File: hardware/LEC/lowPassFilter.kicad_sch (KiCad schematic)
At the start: 3 parts

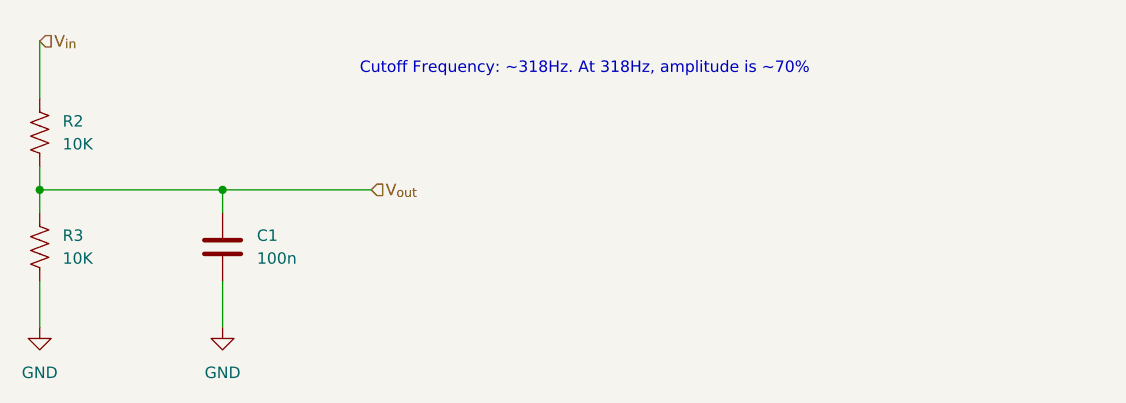
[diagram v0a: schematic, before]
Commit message: Updated LVR selection and other optimizations. Need to update footprints and symbols
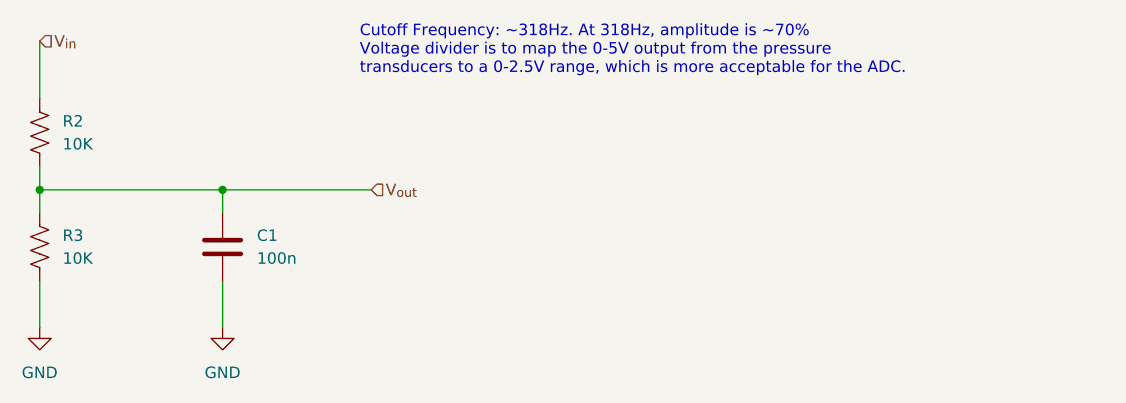
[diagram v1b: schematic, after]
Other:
- note added: "Cutoff Frequency: ~318Hz. At 318Hz, amplitude is ~70% Voltage divider is to map the 0-5V output from the pressure transducers to a 0-2.5V range, which is more acceptable for the ADC."
- note removed: "Cutoff Frequency: ~318Hz. At 318Hz, amplitude is ~70%"
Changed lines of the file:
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@@
     (stroke (width 0) (type default))
   )
-  (text "Cutoff Frequency: ~318Hz. At 318Hz, amplitude is ~70%"
+  (text "Cutoff Frequency: ~318Hz. At 318Hz, amplitude is ~70%\nVoltage divider is to map the 0-5V output from the pressure\ntransducers to a 0-2.5V range, which is more acceptable for the ADC."
     (at 88.9 45.72 0)
     (effects (font (size 1.27 1.27)) (justify left bottom))
@@
           (reference "R3") (unit 1)
         )
+        (path "/c984ce56-a2b4-4cda-8793-153280694173/43e0f5e3-3f54-4d98-bbaa-462e93d257d8"
+          (reference "R4") (unit 1)
+        )
+        (path "/c984ce56-a2b4-4cda-8793-153280694173/c8421286-eac1-4319-8828-3ae62d6cf309"
+          (reference "R6") (unit 1)
+        )
+        (path "/c984ce56-a2b4-4cda-8793-153280694173/7d537dc8-0a6f-4081-8b44-5517c0a70636"
+          (reference "R8") (unit 1)
+        )
+        (path "/c984ce56-a2b4-4cda-8793-153280694173/22bc0796-a1d2-4bdd-adaf-c9789f8654bb"
+          (reference "R10") (unit 1)
+        )
+        (path "/c984ce56-a2b4-4cda-8793-153280694173/ddbe9da2-a7af-420b-9885-57c1b56df261"
+          (reference "R12") (unit 1)
+        )
+        (path "/c984ce56-a2b4-4cda-8793-153280694173/f0feb978-fa39-4938-b0b7-0afa0feb56b9"
+          (reference "R14") (unit 1)
+        )
       )
     )
@@
           (reference "R2") (unit 1)
         )
+        (path "/c984ce56-a2b4-4cda-8793-153280694173/43e0f5e3-3f54-4d98-bbaa-462e93d257d8"
+          (reference "R1") (unit 1)
+        )
+        (path "/c984ce56-a2b4-4cda-8793-153280694173/c8421286-eac1-4319-8828-3ae62d6cf309"
+          (reference "R5") (unit 1)
+        )
+        (path "/c984ce56-a2b4-4cda-8793-153280694173/7d537dc8-0a6f-4081-8b44-5517c0a70636"
+          (reference "R7") (unit 1)
+        )
+        (path "/c984ce56-a2b4-4cda-8793-153280694173/22bc0796-a1d2-4bdd-adaf-c9789f8654bb"
+          (reference "R9") (unit 1)
+        )
+        (path "/c984ce56-a2b4-4cda-8793-153280694173/ddbe9da2-a7af-420b-9885-57c1b56df261"
+          (reference "R11") (unit 1)
+        )
+        (path "/c984ce56-a2b4-4cda-8793-153280694173/f0feb978-fa39-4938-b0b7-0afa0feb56b9"
+          (reference "R13") (unit 1)
+        )
       )
     )
@@
           (reference "C1") (unit 1)
         )
+        (path "/c984ce56-a2b4-4cda-8793-153280694173/43e0f5e3-3f54-4d98-bbaa-462e93d257d8"
+          (reference "C4") (unit 1)
+        )
+        (path "/c984ce56-a2b4-4cda-8793-153280694173/c8421286-eac1-4319-8828-3ae62d6cf309"
+          (reference "C5") (unit 1)
+        )
+        (path "/c984ce56-a2b4-4cda-8793-153280694173/7d537dc8-0a6f-4081-8b44-5517c0a70636"
+          (reference "C6") (unit 1)
+        )
+        (path "/c984ce56-a2b4-4cda-8793-153280694173/22bc0796-a1d2-4bdd-adaf-c9789f8654bb"
+          (reference "C7") (unit 1)
+        )
+        (path "/c984ce56-a2b4-4cda-8793-153280694173/ddbe9da2-a7af-420b-9885-57c1b56df261"
+          (reference "C8") (unit 1)
+        )
+        (path "/c984ce56-a2b4-4cda-8793-153280694173/f0feb978-fa39-4938-b0b7-0afa0feb56b9"
+          (reference "C9") (unit 1)
+        )
       )
     )
@@
   (symbol (lib_id "power:GND") (at 53.34 73.66 0) (unit 1)
     (in_bom yes) (on_board yes) (dnp no) (fields_autoplaced)
-    (property "Reference" "#PWR016" (at 53.34 80.01 0)
+    (property "Reference" "#PWR049" (at 53.34 80.01 0)
       (effects (font (size 1.27 1.27)) hide)
     )
@@
       (project "LEC"
         (path "/c984ce56-a2b4-4cda-8793-153280694173/0e5671ea-d349-45f8-bf6b-96c457441257"
+          (reference "#PWR049") (unit 1)
+        )
+        (path "/c984ce56-a2b4-4cda-8793-153280694173/43e0f5e3-3f54-4d98-bbaa-462e93d257d8"
+          (reference "#PWR03") (unit 1)
+        )
+        (path "/c984ce56-a2b4-4cda-8793-153280694173/c8421286-eac1-4319-8828-3ae62d6cf309"
+          (reference "#PWR04") (unit 1)
+        )
+        (path "/c984ce56-a2b4-4cda-8793-153280694173/7d537dc8-0a6f-4081-8b44-5517c0a70636"
           (reference "#PWR016") (unit 1)
+        )
+        (path "/c984ce56-a2b4-4cda-8793-153280694173/22bc0796-a1d2-4bdd-adaf-c9789f8654bb"
+          (reference "#PWR033") (unit 1)
+        )
+        (path "/c984ce56-a2b4-4cda-8793-153280694173/ddbe9da2-a7af-420b-9885-57c1b56df261"
+          (reference "#PWR021") (unit 1)
+        )
+        (path "/c984ce56-a2b4-4cda-8793-153280694173/f0feb978-fa39-4938-b0b7-0afa0feb56b9"
+          (reference "#PWR023") (unit 1)
         )
       )
@@
           (reference "#PWR019") (unit 1)
         )
-      )
+        (path "/c984ce56-a2b4-4cda-8793-153280694173/43e0f5e3-3f54-4d98-bbaa-462e93d257d8"
+          (reference "#PWR027") (unit 1)
+        )
+        (path "/c984ce56-a2b4-4cda-8793-153280694173/c8421286-eac1-4319-8828-3ae62d6cf309"
+          (reference "#PWR029") (unit 1)
+        )
+        (path "/c984ce56-a2b4-4cda-8793-153280694173/7d537dc8-0a6f-4081-8b44-5517c0a70636"
+          (reference "#PWR031") (unit 1)
+        )
+        (path "/c984ce56-a2b4-4cda-8793-153280694173/22bc0796-a1d2-4bdd-adaf-c9789f8654bb"
+          (reference "#PWR050") (unit 1)
+        )
+        (path "/c984ce56-a2b4-4cda-8793-153280694173/ddbe9da2-a7af-420b-9885-57c1b56df261"
+          (reference "#PWR035") (unit 1)
+        )
+        (path "/c984ce56-a2b4-4cda-8793-153280694173/f0feb978-fa39-4938-b0b7-0afa0feb56b9"
+          (reference "#PWR037") (unit 1)
+        )
+      )

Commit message: Initial commit of PCB files, updated schematic syntax to smooth PCB design workflow. Need to fill ground planes and other necessary updates
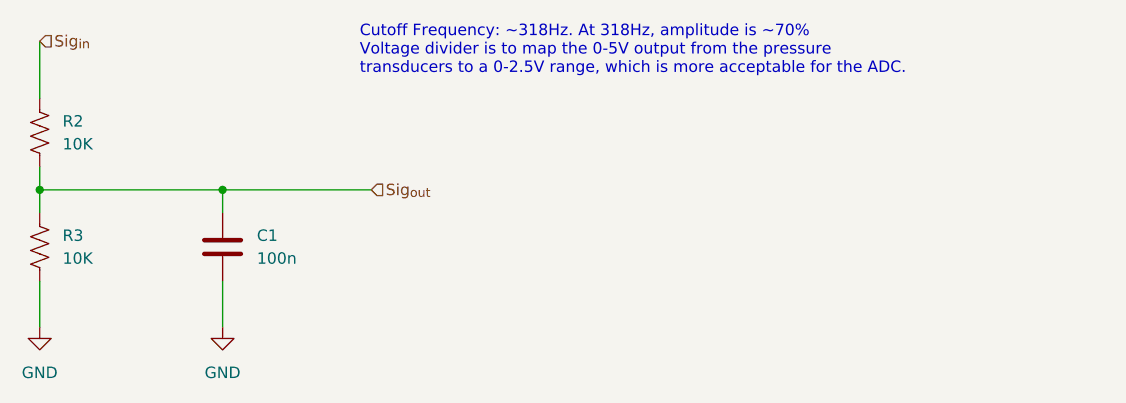
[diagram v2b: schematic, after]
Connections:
- net V_{in} renamed Sig_{in}
- net V_{out} renamed Sig_{out}
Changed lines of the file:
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@@
     (effects (font (size 1.27 1.27)) (justify left bottom))
   )
-  (hierarchical_label "V_{out}" (shape input) (at 90.17 58.42 0) (fields_autoplaced)
+  (hierarchical_label "Sig_{out}" (shape input) (at 90.17 58.42 0) (fields_autoplaced)
     (effects (font (size 1.27 1.27)) (justify left))
   )
-  (hierarchical_label "V_{in}" (shape input) (at 53.34 41.91 0) (fields_autoplaced)
+  (hierarchical_label "Sig_{in}" (shape input) (at 53.34 41.91 0) (fields_autoplaced)
     (effects (font (size 1.27 1.27)) (justify left))
   )

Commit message: Updated schematic documentation, more production files
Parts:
- C1: DigiKey (none) -> https://www.digikey.com/en/products/detail/murata-electroni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; Digikey https://www.digikey.com/en/products/detail/murata-electroni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 -> (none)
- R2, R3: DigiKey (none) -> https://www.digikey.com/en/products/detail/vishay-dale/TNPW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; Digikey https://www.digikey.com/en/products/detail/vishay-dale/TNPW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 -> (none)
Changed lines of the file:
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@@
       (effects (font (size 1.27 1.27)) hide)
     )
-    (property "Digikey" "https://www.digikey.com/en/products/detail/vishay-dale/TNPW060310K0BEEA/1606881" (at 53.34 64.77 0)
+    (property "DigiKey" "https://www.digikey.com/en/products/detail/vishay-dale/TNPW060310K0BEEA/1606881" (at 53.34 64.77 0)
       (effects (font (size 1.27 1.27)) hide)
     )
@@
       (effects (font (size 1.27 1.27)) hide)
     )
-    (property "Digikey" "https://www.digikey.com/en/products/detail/vishay-dale/TNPW060310K0BEEA/1606881" (at 53.34 52.07 0)
+    (property "DigiKey" "https://www.digikey.com/en/products/detail/vishay-dale/TNPW060310K0BEEA/1606881" (at 53.34 52.07 0)
       (effects (font (size 1.27 1.27)) hide)
     )
@@
       (effects (font (size 1.27 1.27)) hide)
     )
-    (property "Digikey" "https://www.digikey.com/en/products/detail/murata-electronics/GRM3195C1H104JA05D/13531811" (at 73.66 64.77 0)
+    (property "DigiKey" "https://www.digikey.com/en/products/detail/murata-electronics/GRM3195C1H104JA05D/13531811" (at 73.66 64.77 0)
       (effects (font (size 1.27 1.27)) hide)
     )
